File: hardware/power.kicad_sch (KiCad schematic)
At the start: 4 parts, among them U4 TPSM828214SILR

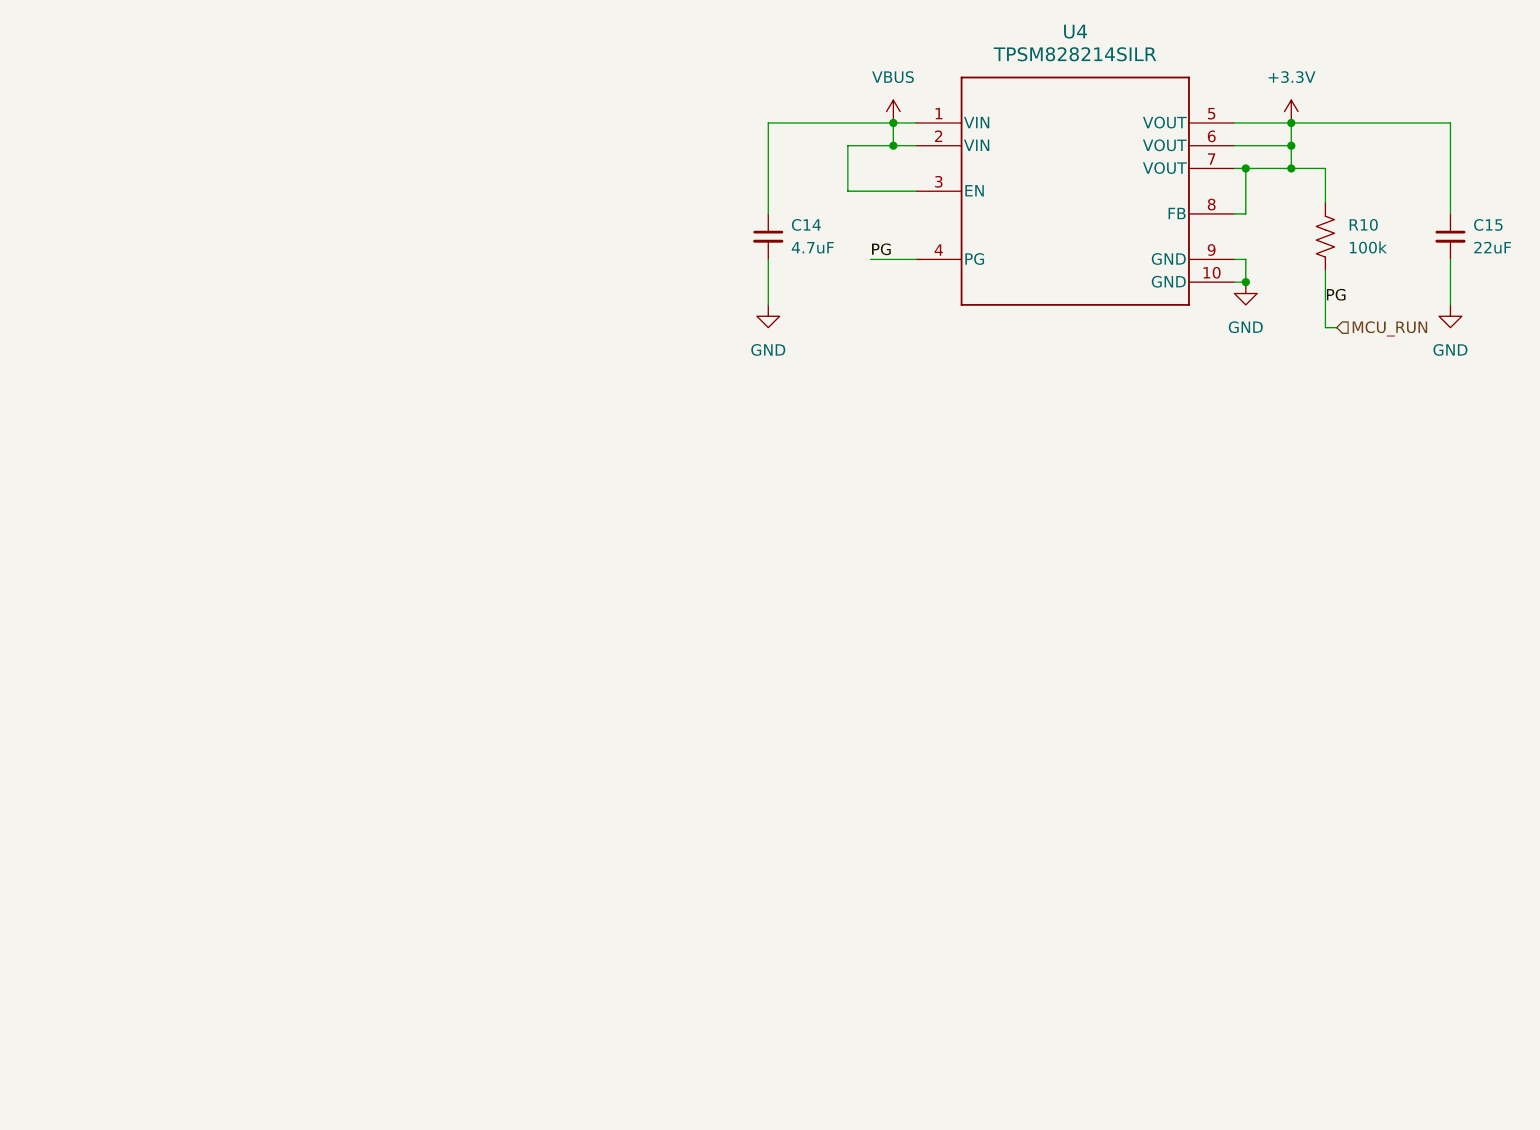
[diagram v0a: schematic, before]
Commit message: started placing leds
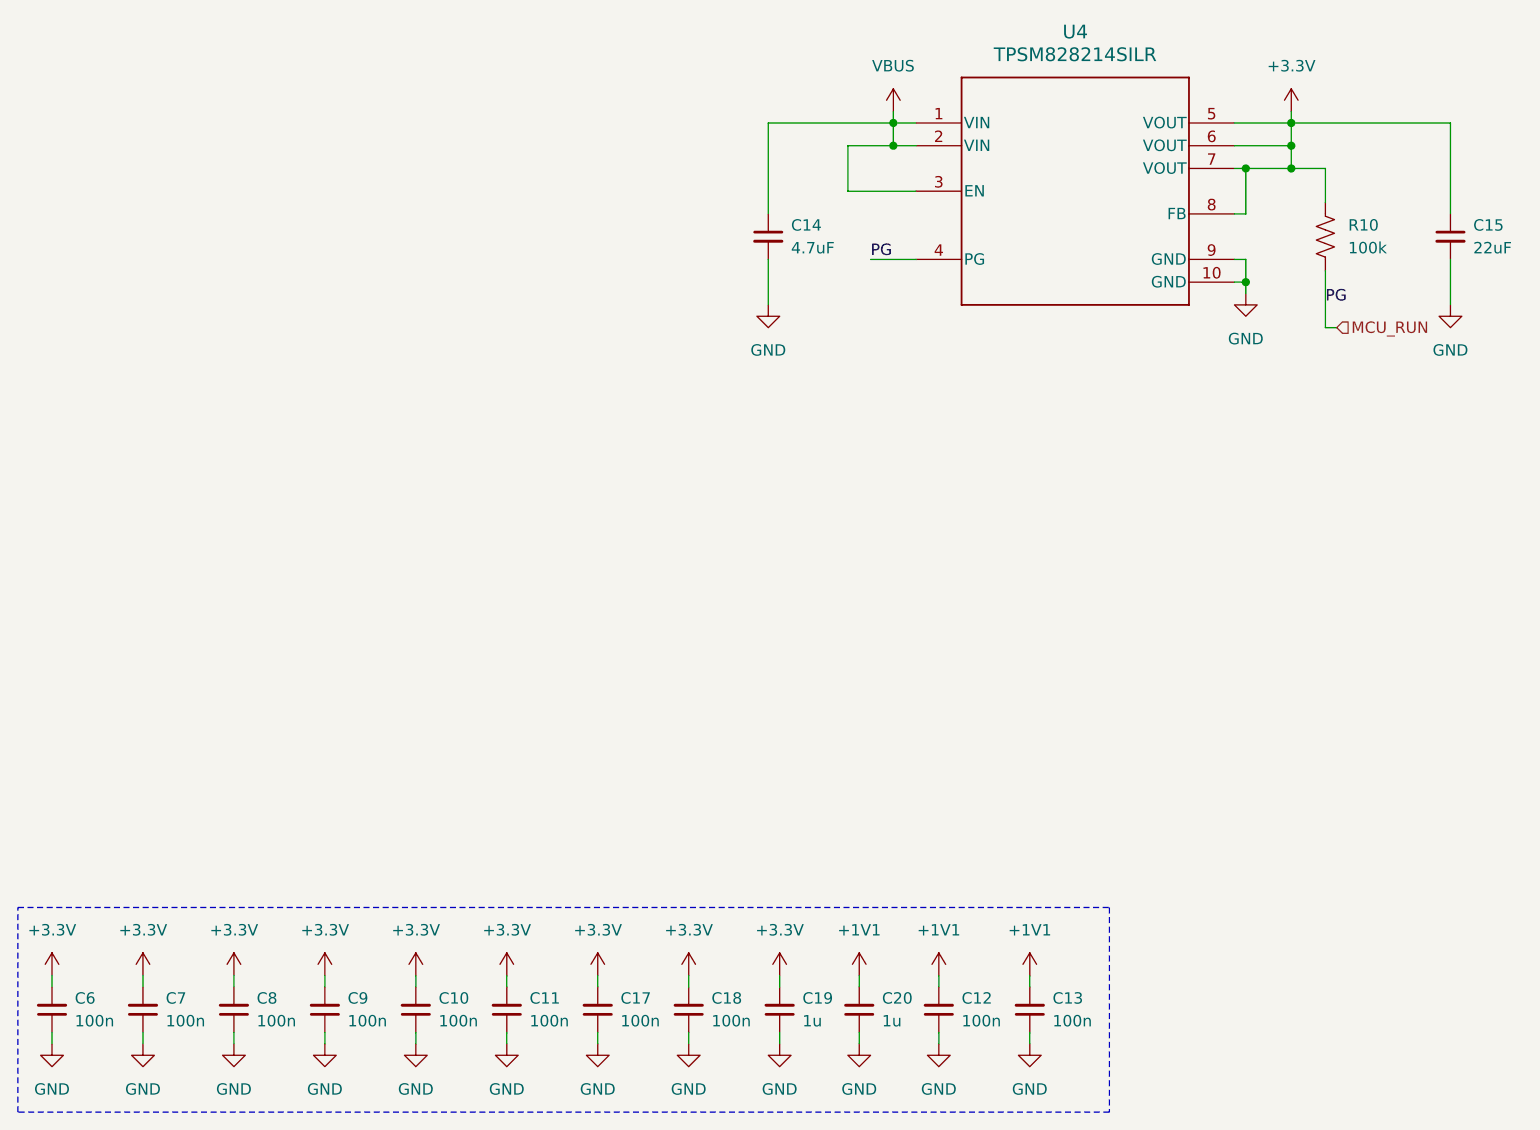
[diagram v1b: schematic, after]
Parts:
- added C10, C11, C12, C13, C17, C18, C6, C7, C8, C9: 100n, symbol Device:C_Small
- added C19, C20: 1u, symbol Device:C_Small
- U4: footprint SIL0010D-MFG -> LBD_Footprints:TPSM828214SILR
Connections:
- net +3.3V: now also C10.2, C11.2, C17.2, C18.2, C19.2, C6.2, C7.2, C8.2, C9.2
- net GND: now also C10.1, C11.1, C12.1, C13.1, C17.1, C18.1, C19.1, C20.1, C6.1, C7.1, C8.1, C9.1
- new net +1V1: C12.2, C13.2, C20.2
